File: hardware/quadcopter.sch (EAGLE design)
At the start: 60 parts, among them J1 AVR_SPI_PRG_6NS, J2 HEADER-4POS-2X2-0.1IN-FEMALE-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, J3 HEADER-10POSTH-254X10, J4 HEADER-4POS-2X2-0.1IN-FEMALE-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, Q3 MOSFET-FET-SI2302CDS-T1-E3CT-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, Q4 MOSFET-FET-SI2302CDS-T1-E3CT-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, Q5 MOSFET-FET-SI2302CDS-T1-E3CT-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, Q6 MOSFET-FET-SI2302CDS-T1-E3CT-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, U1 ATMEGA128RFA1, U2 IMU-LSM6DSOXTR-497-18367-1-ND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, Y1 CRYSTAL5X3

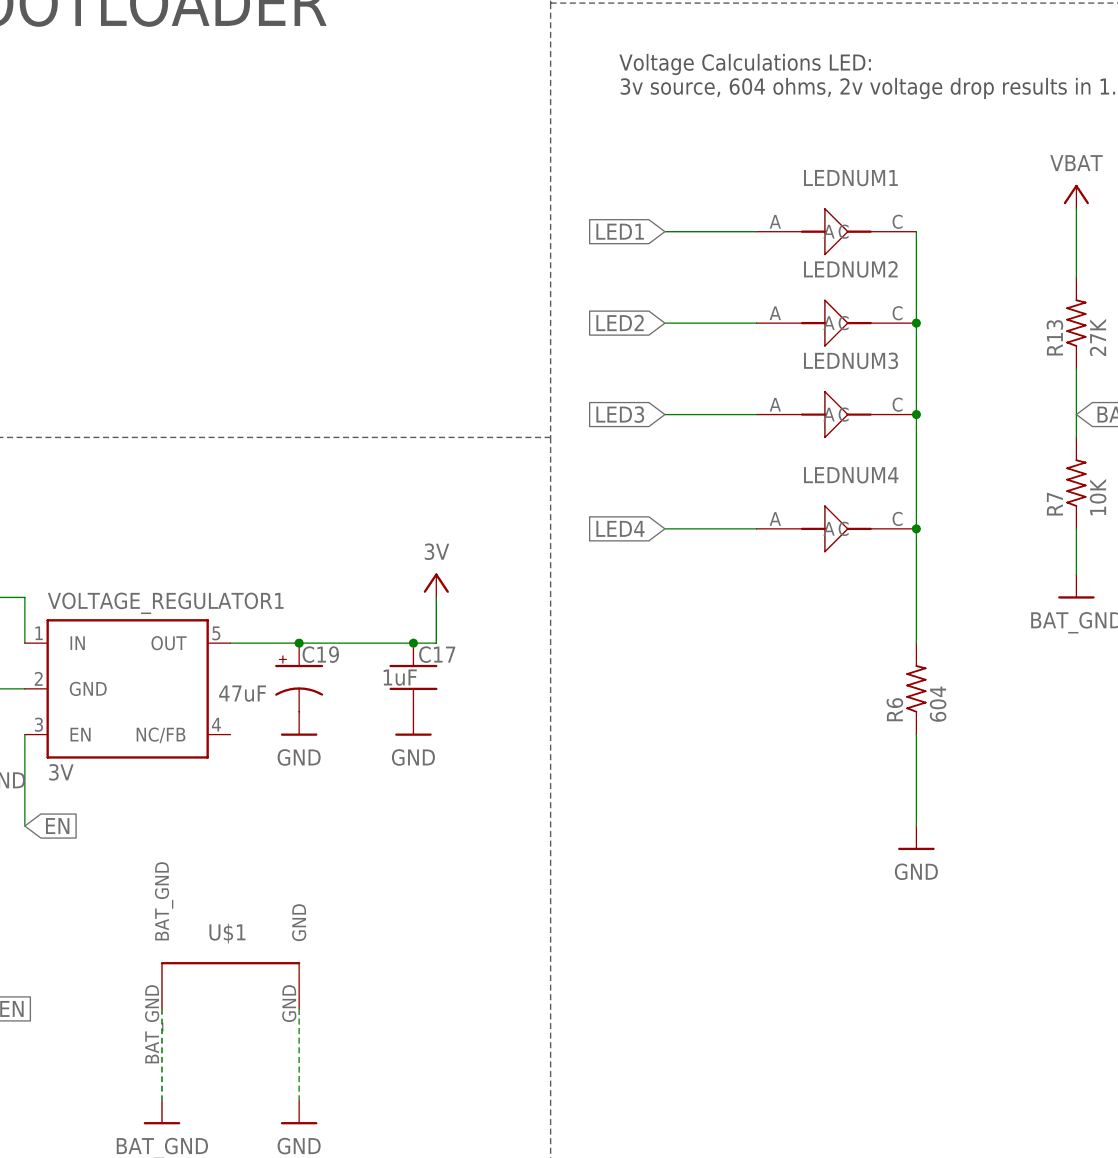
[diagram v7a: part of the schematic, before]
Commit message: fixing LED values, more library dependencies
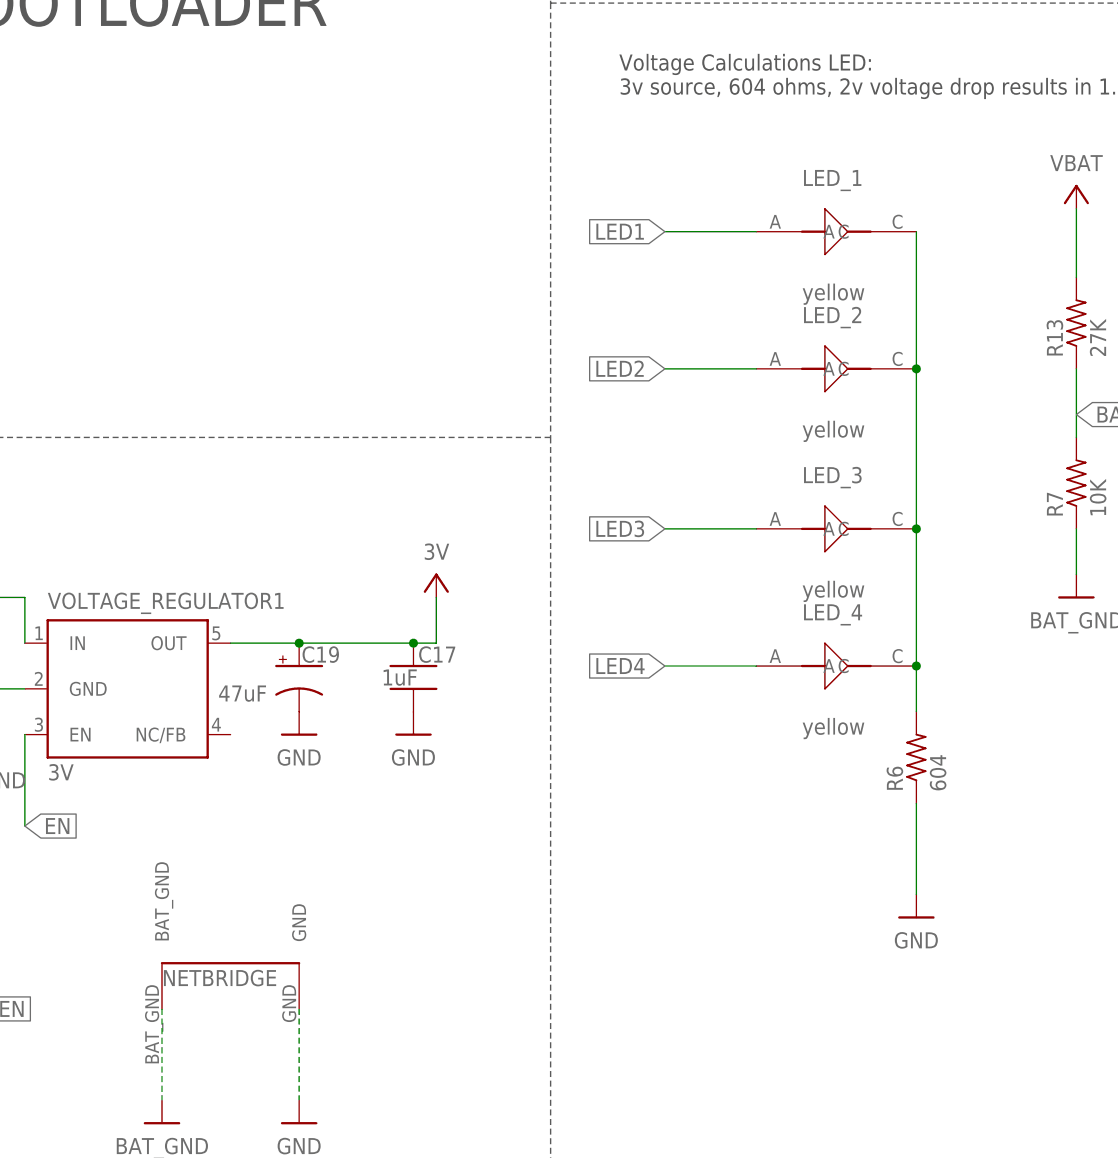
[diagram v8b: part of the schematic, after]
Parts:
- removed LEDNUM2, LEDNUM3: LED_YELLOW, LED:LED_YELLOW
- added LED_2, LED_4: yellow, LED:LED_YELLOW
- LED_1, LED_3: value LED_YELLOW -> yellow
- renumbered LEDNUM1 to LED_1, LEDNUM4 to LED_3, U$1 to NETBRIDGE
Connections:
- net LED2: now also LED_2.A; no longer LEDNUM2.A
- net LED3: now also LED_3.A; no longer LEDNUM3.A
- net LED4: now also LED_4.A; no longer LED_3.A
- net N$12: now also LED_2.C, LED_4.C; no longer LEDNUM2.C, LEDNUM3.C
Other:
- moved on the sheet: R6
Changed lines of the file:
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@@
 <part name="GND43" library="quadparts_prebuilt_2022" deviceset="GND" device=""/>
 <part name="P+19" library="quadparts_prebuilt_2022" deviceset="3V" device=""/>
-<part name="LEDNUM4" library="LED" library_urn="urn:adsk.wipprod:fs.file:vf.dgQ34RYLRkWtLog4lTO-XQ" deviceset="LED_YELLOW" device=""/>
-<part name="LEDNUM3" library="LED" library_urn="urn:adsk.wipprod:fs.file:vf.dgQ34RYLRkWtLog4lTO-XQ" deviceset="LED_YELLOW" device=""/>
-<part name="LEDNUM2" library="LED" library_urn="urn:adsk.wipprod:fs.file:vf.dgQ34RYLRkWtLog4lTO-XQ" deviceset="LED_YELLOW" device=""/>
-<part name="LEDNUM1" library="LED" library_urn="urn:adsk.wipprod:fs.file:vf.dgQ34RYLRkWtLog4lTO-XQ" deviceset="LED_YELLOW" device=""/>
-<part name="U$1" library="custom_v9" library_urn="urn:adsk.wipprod:fs.file:vf.hOpq96TzSi2cy5Li20AtXQ" deviceset="NETBRIDGE" device=""/>
+<part name="NETBRIDGE" library="custom_v9" library_urn="urn:adsk.wipprod:fs.file:vf.hOpq96TzSi2cy5Li20AtXQ" deviceset="NETBRIDGE" device=""/>
 <part name="GND17" library="quadparts_prebuilt_2022" deviceset="BAT_GND" device=""/>
 <part name="GND18" library="quadparts_prebuilt_2022" deviceset="GND" device=""/>
+<part name="LED_1" library="LED" deviceset="LED_YELLOW" device="" value="yellow"/>
+<part name="LED_2" library="LED" deviceset="LED_YELLOW" device="" value="yellow"/>
+<part name="LED_3" library="LED" deviceset="LED_YELLOW" device="" value="yellow"/>
+<part name="LED_4" library="LED" deviceset="LED_YELLOW" device="" value="yellow"/>
 </parts>
 <sheets>
@@
 <attribute name="NAME" x="155.702" y="55.88" size="1.778" layer="95" rot="R180"/>
 </instance>
-<instance part="GND23" gate="1" x="104.14" y="-71.12" smashed="yes">
-<attribute name="VALUE" x="104.14" y="-73.66" size="1.778" layer="96" align="center"/>
-</instance>
-<instance part="R6" gate="G$1" x="104.14" y="-53.34" smashed="yes" rot="R90">
-<attribute name="VALUE" x="107.442" y="-57.15" size="1.778" layer="96" rot="R90"/>
-<attribute name="NAME" x="102.6414" y="-57.15" size="1.778" layer="95" rot="R90"/>
+<instance part="GND23" gate="1" x="104.14" y="-78.74" smashed="yes">
+<attribute name="VALUE" x="104.14" y="-81.28" size="1.778" layer="96" align="center"/>
+</instance>
+<instance part="R6" gate="G$1" x="104.14" y="-60.96" smashed="yes" rot="R90">
+<attribute name="VALUE" x="107.442" y="-64.77" size="1.778" layer="96" rot="R90"/>
+<attribute name="NAME" x="102.6414" y="-64.77" size="1.778" layer="95" rot="R90"/>
 </instance>
 <instance part="GND37" gate="1" x="121.92" y="-43.18" smashed="yes">
@@
 <attribute name="VALUE" x="50.8" y="-38.1" size="1.778" layer="96" rot="R180" align="center"/>
 </instance>
-<instance part="LEDNUM4" gate="G$1" x="93.98" y="-35.56" smashed="yes">
-<attribute name="NAME" x="91.44" y="-30.48" size="1.778" layer="95"/>
-</instance>
-<instance part="LEDNUM3" gate="G$1" x="93.98" y="-22.86" smashed="yes">
-<attribute name="NAME" x="91.44" y="-17.78" size="1.778" layer="95"/>
-</instance>
-<instance part="LEDNUM2" gate="G$1" x="93.98" y="-12.7" smashed="yes">
-<attribute name="NAME" x="91.44" y="-7.62" size="1.778" layer="95"/>
-</instance>
-<instance part="LEDNUM1" gate="G$1" x="93.98" y="-2.54" smashed="yes">
-<attribute name="NAME" x="91.44" y="2.54" size="1.778" layer="95"/>
-</instance>
-<instance part="U$1" gate="G$1" x="27.94" y="-86.36" smashed="yes">
-<attribute name="NAME" x="25.4" y="-81.28" size="1.778" layer="95"/>
+<instance part="NETBRIDGE" gate="G$1" x="27.94" y="-86.36" smashed="yes">
+<attribute name="NAME" x="20.32" y="-86.36" size="1.778" layer="95"/>
 </instance>
 <instance part="GND17" gate="1" x="20.32" y="-101.6" smashed="yes">
@@
 <instance part="GND18" gate="1" x="35.56" y="-101.6" smashed="yes">
 <attribute name="VALUE" x="35.56" y="-104.14" size="1.778" layer="96" align="center"/>
+</instance>
+<instance part="LED_1" gate="G$1" x="93.98" y="-2.54" smashed="yes">
+<attribute name="NAME" x="91.44" y="2.54" size="1.778" layer="95"/>
+<attribute name="VALUE" x="91.44" y="-10.16" size="1.778" layer="96"/>
+</instance>
+<instance part="LED_2" gate="G$1" x="93.98" y="-17.78" smashed="yes">
+<attribute name="NAME" x="91.44" y="-12.7" size="1.778" layer="95"/>
+<attribute name="VALUE" x="91.44" y="-25.4" size="1.778" layer="96"/>
+</instance>
+<instance part="LED_3" gate="G$1" x="93.98" y="-35.56" smashed="yes">
+<attribute name="NAME" x="91.44" y="-30.48" size="1.778" layer="95"/>
+<attribute name="VALUE" x="91.44" y="-43.18" size="1.778" layer="96"/>
+</instance>
+<instance part="LED_4" gate="G$1" x="93.98" y="-50.8" smashed="yes">
+<attribute name="NAME" x="91.44" y="-45.72" size="1.778" layer="95"/>
+<attribute name="VALUE" x="91.44" y="-58.42" size="1.778" layer="96"/>
 </instance>
 </instances>
@@
 </segment>
 <segment>
-<wire x1="104.14" y1="-58.42" x2="104.14" y2="-68.58" width="0.1524" layer="91"/>
+<wire x1="104.14" y1="-66.04" x2="104.14" y2="-76.2" width="0.1524" layer="91"/>
 <pinref part="GND23" gate="1" pin="GND"/>
 <pinref part="R6" gate="G$1" pin="1"/>
@@
 </segment>
 <segment>
-<pinref part="U$1" gate="G$1" pin="GND"/>
+<pinref part="NETBRIDGE" gate="G$1" pin="GND"/>
 <wire x1="35.56" y1="-88.9" x2="35.56" y2="-99.06" width="0.1524" layer="91" style="longdash"/>
 <pinref part="GND18" gate="1" pin="GND"/>
@@
 </segment>
 <segment>
-<pinref part="LEDNUM2" gate="G$1" pin="A"/>
-<wire x1="86.36" y1="-12.7" x2="76.2" y2="-12.7" width="0.1524" layer="91"/>
-<label x="76.2" y="-12.7" size="1.778" layer="95" rot="MR0" xref="yes"/>
+<wire x1="86.36" y1="-17.78" x2="76.2" y2="-17.78" width="0.1524" layer="91"/>
+<label x="76.2" y="-17.78" size="1.778" layer="95" rot="MR0" xref="yes"/>
+<pinref part="LED_2" gate="G$1" pin="A"/>
 </segment>
 </net>
@@
 </segment>
 <segment>
-<pinref part="LEDNUM3" gate="G$1" pin="A"/>
-<wire x1="86.36" y1="-22.86" x2="76.2" y2="-22.86" width="0.1524" layer="91"/>
-<label x="76.2" y="-22.86" size="1.778" layer="95" rot="MR0" xref="yes"/>
+<wire x1="86.36" y1="-35.56" x2="76.2" y2="-35.56" width="0.1524" layer="91"/>
+<label x="76.2" y="-35.56" size="1.778" layer="95" rot="MR0" xref="yes"/>
+<pinref part="LED_3" gate="G$1" pin="A"/>
 </segment>
 </net>
@@
 </segment>
 <segment>
-<pinref part="LEDNUM4" gate="G$1" pin="A"/>
-<wire x1="86.36" y1="-35.56" x2="76.2" y2="-35.56" width="0.1524" layer="91"/>
-<label x="76.2" y="-35.56" size="1.778" layer="95" rot="MR0" xref="yes"/>
+<wire x1="86.36" y1="-50.8" x2="76.2" y2="-50.8" width="0.1524" layer="91"/>
+<label x="76.2" y="-50.8" size="1.778" layer="95" rot="MR0" xref="yes"/>
+<pinref part="LED_4" gate="G$1" pin="A"/>
 </segment>
 </net>
@@
 </segment>
 <segment>
-<pinref part="U$1" gate="G$1" pin="BAT_GND"/>
+<pinref part="NETBRIDGE" gate="G$1" pin="BAT_GND"/>
 <wire x1="20.32" y1="-88.9" x2="20.32" y2="-99.06" width="0.1524" layer="91" style="longdash"/>
 <pinref part="GND17" gate="1" pin="BAT_GND"/>
@@
 </segment>
 <segment>
-<pinref part="LEDNUM1" gate="G$1" pin="A"/>
 <wire x1="86.36" y1="-2.54" x2="76.2" y2="-2.54" width="0.1524" layer="91"/>
 <label x="76.2" y="-2.54" size="1.778" layer="95" rot="MR0" xref="yes"/>
+<pinref part="LED_1" gate="G$1" pin="A"/>
 </segment>
 </net>
@@
 </segment>
 </net>
-<net name="N$12" class="0">
-<segment>
-<pinref part="LEDNUM1" gate="G$1" pin="C"/>
-<wire x1="104.14" y1="-2.54" x2="104.14" y2="-12.7" width="0.1524" layer="91"/>
-<pinref part="LEDNUM4" gate="G$1" pin="C"/>
-<wire x1="104.14" y1="-12.7" x2="104.14" y2="-22.86" width="0.1524" layer="91"/>
-<wire x1="104.14" y1="-22.86" x2="104.14" y2="-35.56" width="0.1524" layer="91"/>
-<wire x1="104.14" y1="-35.56" x2="104.14" y2="-48.26" width="0.1524" layer="91"/>
-<pinref part="LEDNUM3" gate="G$1" pin="C"/>
-<pinref part="LEDNUM2" gate="G$1" pin="C"/>
-<pinref part="R6" gate="G$1" pin="2"/>
-<junction x="104.14" y="-12.7"/>
-<junction x="104.14" y="-35.56"/>
-<junction x="104.14" y="-22.86"/>
-</segment>
-</net>
 <net name="N$13" class="0">
 <segment>
@@
 </segment>
 </net>
+<net name="N$12" class="0">
+<segment>
+<pinref part="LED_1" gate="G$1" pin="C"/>
+<wire x1="104.14" y1="-2.54" x2="104.14" y2="-17.78" width="0.1524" layer="91"/>
+<pinref part="R6" gate="G$1" pin="2"/>
+<pinref part="LED_2" gate="G$1" pin="C"/>
+<wire x1="104.14" y1="-17.78" x2="104.14" y2="-35.56" width="0.1524" layer="91"/>
+<junction x="104.14" y="-17.78"/>
+<pinref part="LED_3" gate="G$1" pin="C"/>
+<wire x1="104.14" y1="-35.56" x2="104.14" y2="-50.8" width="0.1524" layer="91"/>
+<junction x="104.14" y="-35.56"/>
+<pinref part="LED_4" gate="G$1" pin="C"/>
+<wire x1="104.14" y1="-50.8" x2="104.14" y2="-55.88" width="0.1524" layer="91"/>
+<junction x="104.14" y="-50.8"/>
+</segment>
+</net>
